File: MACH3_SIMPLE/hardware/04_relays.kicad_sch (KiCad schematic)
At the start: 66 parts, among them J40 Relay A, J41 Relay B, J42 Relay C, J43 Relay D, J44 Relay E, J45 Relay F, J50 RS232 RX TX GND, J60 ICSP, K1 JQC-3FF-024-1Z, K2 JQC-3FF-024-1Z, K3 JQC-3FF-024-1Z, K4 JQC-3FF-024-1Z, K5 JQC-3FF-024-1Z, K6 JQC-3FF-024-1Z, Q1 2N7002, Q2 2N7002, Q3 2N7002, Q4 2N7002, Q5 2N7002, Q6 2N7002, U20 MAX3232, U21 ATmega328P-AU, Y1 16MHz

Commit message: MACH3-SIMPLE A1: on-board 5 V, isolated VFD port, four A0 fixes
Power: the 5 V input terminal is gone. An LM2596S-5.0 buck makes +5V from
V24, and the whole supply sits in the top-right corner beside the 24 V
terminal, away from the MCU crystal and the port lines.

Spindle: new J5 (AVI ACM FWD REV DCM). Port 2 pins 7/8/9 go through a
74HC14 to a PC847; the VFD side runs from a B2412S isolated module with a
78L05 reference, a two-pole RC filter and an LM358 trimmed to 10.0 V. It
has its own SP_ACM pour, and the board is routed in two passes so no
board-side copper enters it; autoroute.py barrier checks that and fab.sh
refuses Gerbers without it.

Fixes to A0:
- Q1-Q6 had drain and source swapped; every relay was stuck on through
  the body diode. check_design.py now checks MOSFET orientation.
- The top-edge legends were reversed (+24 over 0V, +5 over MPG B, EMG over
  X home). Signals now follow the printed order, one word per screw.
- PC847 was on a SOIC-16 footprint no PC847 fits; now SMD DIP-16.
- The promised reverse diodes across the input opto LEDs were missing;
  added as D20-D25, with the input channels laid out per screw.

ERC 0, structural checks pass, DRC 0 errors / 0 unconnected / 0 parity,
barrier clean. Not built or powered.

Co-Authored-By: Claude Opus 5.5 <noreply@anthropic.com>
Claude-Session: https://claude.ai/code/session_01MByiLT2xCcbGPkgCYQy33q
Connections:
- net GND: now also Q1.2 (S), Q2.2 (S), Q3.2 (S), Q4.2 (S), Q5.2 (S), Q6.2 (S); no longer Q1.3 (D), Q2.3 (D), Q3.3 (D), Q4.3 (D), Q5.3 (D), Q6.3 (D)
- net RELC_A: now also Q1.3 (D); no longer Q1.2 (S)
- net RELC_B: now also Q2.3 (D); no longer Q2.2 (S)
- net RELC_C: now also Q3.3 (D); no longer Q3.2 (S)
- net RELC_D: now also Q4.3 (D); no longer Q4.2 (S)
- net RELC_E: now also Q5.3 (D); no longer Q5.2 (S)
- net RELC_F: now also Q6.3 (D); no longer Q6.2 (S)

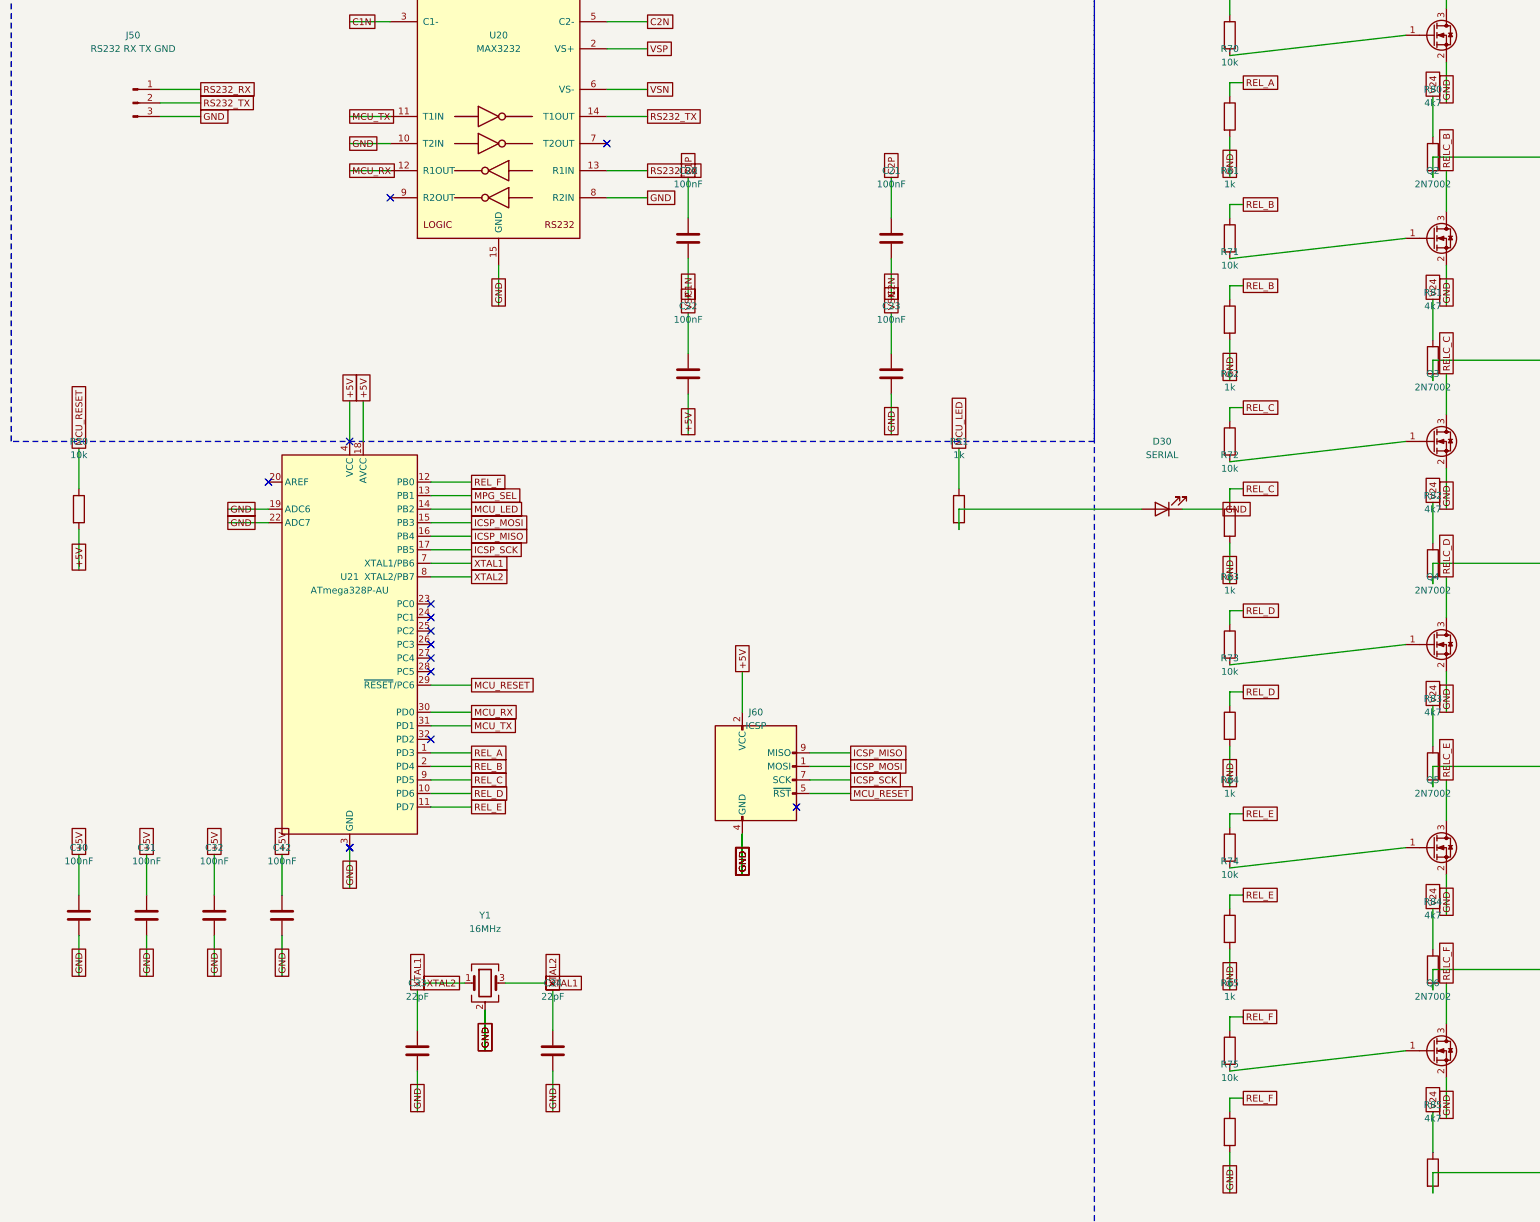
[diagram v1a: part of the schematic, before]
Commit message: MACH3-SIMPLE A1: design-review fixes and options
- Relay terminals labelled: RELAY A-F and NO/COM/NC per screw on the back
  silkscreen, RELAY A-F on the front (were on F.Fab only, not printed).
- R80-R85 4k7 -> 10k: 103 mW in a 100 mW 0603 on 24 V.
- Axis buffers fitted as 74AC245 (same pads) for opto-input drivers.
- J4 is 4-way: fused +24/0V for the sensors beside +24/0V in.
- C2 47 uF 50 V: 100 uF 50 V is not made in 6.3 x 7.7.
- Function labels (5V, 24V, SERIAL, A-F, 10V ADJ), test points GND/5V/24V
  and ACM/12V/AVI, dashed ISOLATED line round the VFD side, MCU heading
  moved beside the MCU.
- Buck switch node hand-drawn and locked: 14 mm top layer, no vias.
- F3 200 mA PTC on the handwheel +5V; 10 nF on MCU reset.
- Spare opto channel as VFD AUX output (port 2 pin 6); J5 is 6-way.
- autoroute.py keeps locked tracks through imports; route_one.py for a
  connection the router leaves open.

ERC 0, structural checks pass, DRC 0 errors / 0 unconnected / 0 parity,
barrier clean. Not built or powered.

Co-Authored-By: Claude Opus 5.5 <noreply@anthropic.com>
Claude-Session: https://claude.ai/code/session_01MByiLT2xCcbGPkgCYQy33q
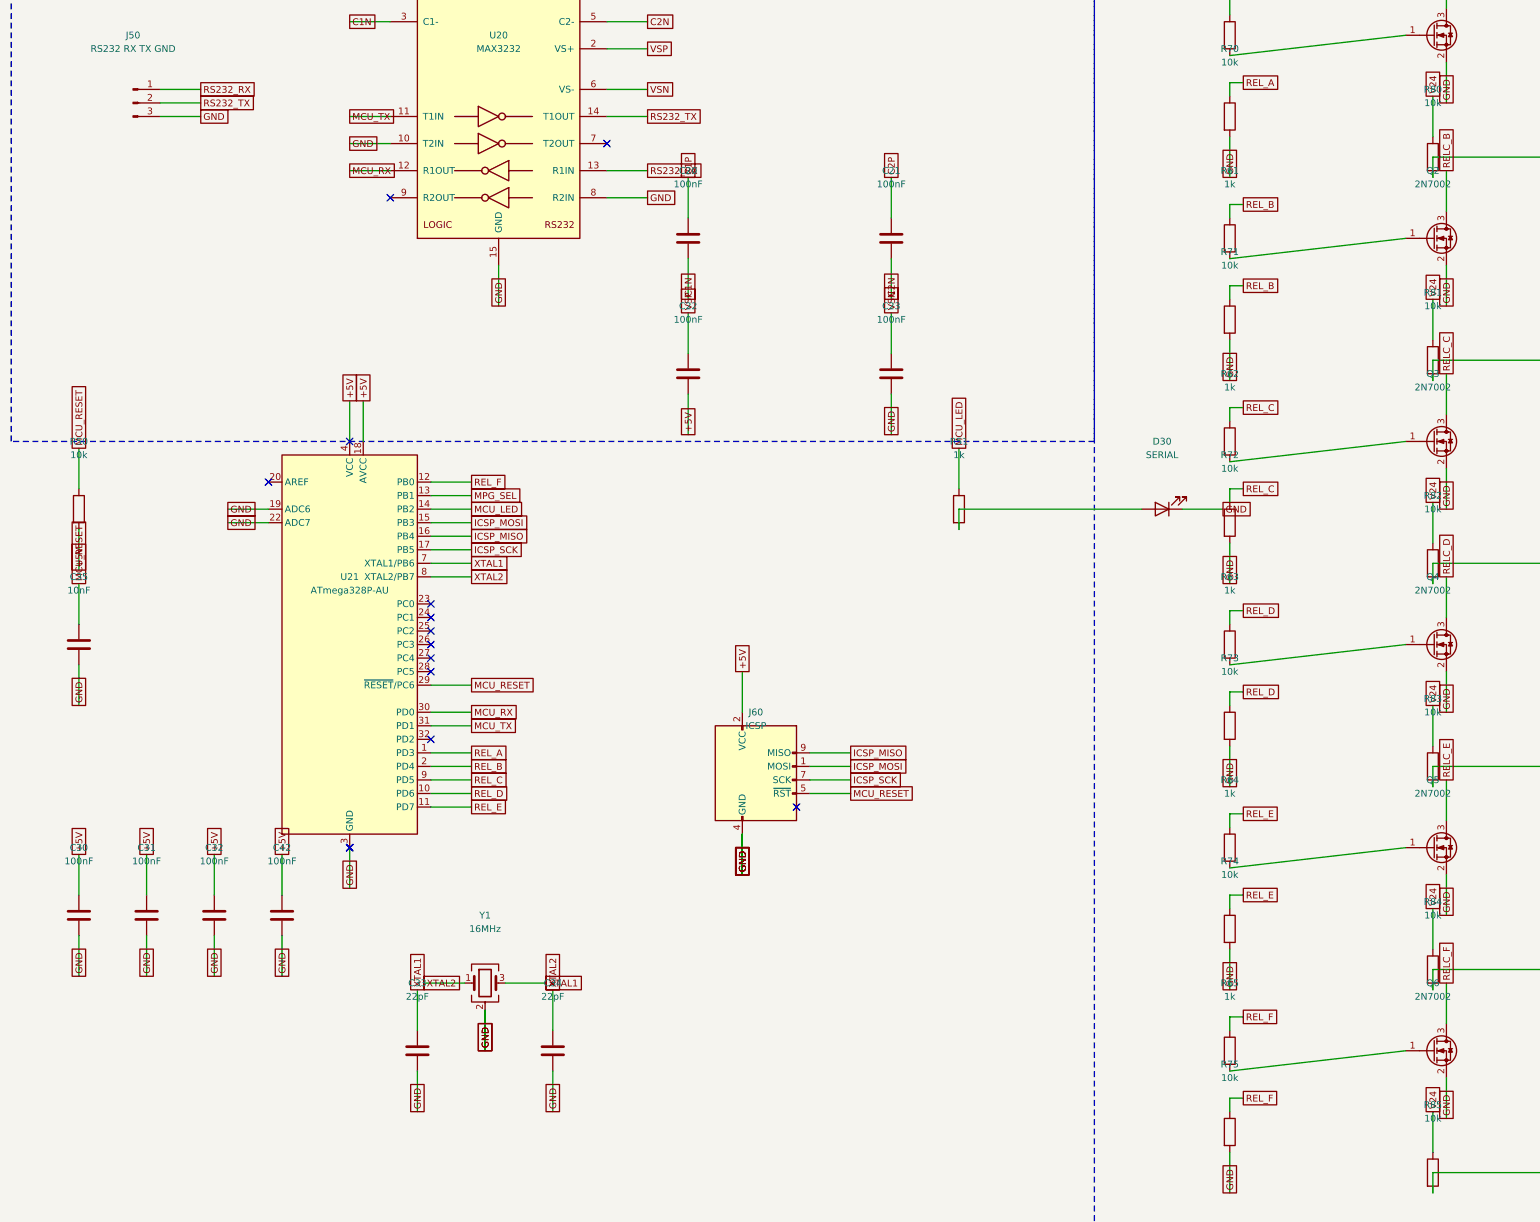
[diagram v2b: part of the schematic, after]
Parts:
- added C35: 10nF, Capacitor_SMD:C_0603_1608Metric, symbol Device:C
- R80, R81, R82, R83, R84, R85: value 4k7 -> 10k
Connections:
- net GND: now also C35.2
- net MCU_RESET: now also C35.1
